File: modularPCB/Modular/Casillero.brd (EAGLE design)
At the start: 100 x 80 mm, 33 parts

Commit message: Actualización de pcbs
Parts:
- removed ALARMA, DISPONIBLE, EMISOR, LED1, LED2, LED3, OCUPADO, RECEPTOR: (no value), led:LED3MM
- removed CHAPA-DATA, CHAPA-VOL: (no value), pinhead:1X02
- removed D1: 1N4004, diode:DO41-10
- removed R-ALARMA, R-DISPONIBLE, R-GAL, R-INFRA-LED, R-OCUPADO, R-UL: 220, rcl:0204/7
- removed R-CHAPA, R-G1, R-G2: 1k, rcl:0204/7
- removed R-CHAPA2: 330, rcl:0204/7
- removed R-EMISOR: 380, rcl:0204/7
- removed R-INFRA, R-RECEPTOR: 22K, rcl:0204/7
- removed U$2: ULTRASONICO, MODULAR:ULTRASONICO
- removed U$4, U$6: 2N2222, MODULAR:2N2222
- removed U$5: RELEY, MODULAR:RELEY
- added JP2, JP3: (no value), pinhead:1X01
- added R-B, R-G, R-R: 220, rcl:0204/7
- added SG1: F/CM12P, buzzer:F/CM12P
- added SV1, SV2: (no value), con-lstb:MA04-2
- added X1, X7: 22-23-2041, con-molex:22-23-2041
- added X2, X3: 22-23-2031, con-molex:22-23-2031
- added X4, X5, X6: 22-23-2021, con-molex:22-23-2021
- JP1: device pinhead:1X03 -> pinhead:1X01
- U$3: value HX-711 -> LEDRGB; device MODULAR:HX-711 -> MODULAR:LEDRGB
- moved U$3 128.0 mm to (75.9, 22.9), turned to 90 degrees
- moved SENSADO 126.4 mm to (68.3, 11.4), turned to 270 degrees
- moved R-SENSADO 113.4 mm to (68.3, 6.35), turned to 180 degrees
- moved JP1 68.9 mm to (45.7, 12.7)
- moved U$1 66.5 mm to (38.1, 40.6), turned to 90 degrees
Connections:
- removed net DATO-CHAPA: CHAPA-DATA.1, R-CHAPA2.2, U$1.D27
- removed net DT-GALGA: U$1.D18, U$3.DT
- removed net ECHO-ULTRASONICO: U$1.D22, U$2.ECHO
- removed net GND1: U$1.GND@1
- removed net LIBRE: U$1.D15
- removed net LIBRE1: U$1.D5
- removed net LIBRE2: U$1.D25
- removed net N$1: LED1.K, R-UL.2
- removed net N$10: D1.A, U$4.C, U$5.B1
- removed net N$13: JP1.1, U$3.A+
- removed net N$14: JP1.2, R-G1.2, U$3.E-
- removed net N$15: JP1.3, R-G2.2, U$3.E+
- removed net N$16: R-G1.1, R-G2.1, U$3.A-
- removed net N$20: EMISOR.A, R-EMISOR.1
- removed net N$24: CHAPA-VOL.1, U$5.NA
- removed net N$30: R-RECEPTOR.1, RECEPTOR.K, U$6.B
- removed net N$31: LED3.A, R-INFRA-LED.1
- removed net N$32: DISPONIBLE.K, R-DISPONIBLE.2
- removed net N$33: ALARMA.K, R-ALARMA.2
- removed net N$34: R-SENSADO.2, SENSADO.K
- removed net N$8: LED2.K, R-GAL.2
- removed net N$9: R-CHAPA.1, U$4.B
- removed net PULSO-ALARMA: ALARMA.A, U$1.D14
- removed net PULSO-CHAPA: R-CHAPA.2, U$1.D26
- removed net PULSO-DISPONIBLE: DISPONIBLE.A, U$1.D12
- removed net PULSO-GALGA: LED2.A, U$1.D21
- removed net PULSO-INFRA: R-INFRA-LED.2, R-INFRA.1, U$1.D2, U$6.E
- removed net PULSO-OCUPADO: OCUPADO.A, U$1.D13
- removed net PULSO-SENSADO: SENSADO.A, U$1.D4
- removed net PULSO-ULTRASONICO: LED1.A, U$1.D32
- removed net PURA-ENTRADA: U$1.D34
- removed net SCK-GALGA: U$1.D19, U$3.SCK
- removed net TRIG-ULTRASONICO: U$1.D23, U$2.TRIG
- removed net VF: D1.C, U$5.B2, U$5.IN
- new net BUZZER: SG1.+, U$1.D27
- new net CERRADURA_CTRL: U$1.D25, X6.2
- new net CERRADURA_VCC: U$1.D26, X6.1
- new net GA_DT: U$1.D19, X3.2
- new net GA_LED: U$1.D21, X3.1
- new net GA_SCK: U$1.D18, X3.3
- new net IR: JP1.1, U$1.D34
- new net LCD_SCL: U$1.D5, X5.2
- new net LCD_SDA: U$1.D15, X5.1
- new net LED_B: R-B.2, U$1.D14, X1.4, X7.2
- new net LED_G: R-G.2, U$1.D12, X1.3, X7.3
- new net LED_R: R-R.2, U$1.D13, X1.2, X7.4
- new net N$2: R-R.1, U$3.R
- new net N$4: R-B.1, U$3.B
- new net N$7: R-SENSADO.1, SENSADO.A
- new net SENSADO_LED: JP2.1, R-SENSADO.2, U$1.D4, X4.2
- new net UL_ECHO: U$1.D22, X2.2
- new net UL_LED: U$1.D32, X2.1
- new net UL_TRG: U$1.D23, X2.3
- new net WIFI_LED: U$1.D2
- net 3V3: now also SV1.1, SV1.3, SV1.5, SV1.7; no longer CHAPA-DATA.2, R-EMISOR.2, R-RECEPTOR.2, U$3.VCC
- net GND: now also SENSADO.K, SG1.-, SV1.2, SV1.4, SV1.6, SV1.8, SV2.2, SV2.4, SV2.6, SV2.8, U$1.GND@1, X1.1, X4.1, X7.1; no longer CHAPA-VOL.2, EMISOR.K, LED3.K, R-ALARMA.1, R-CHAPA2.1, R-DISPONIBLE.1, R-GAL.1, R-INFRA.2, R-OCUPADO.1, R-SENSADO.1, R-UL.1, RECEPTOR.A, U$2.GND, U$4.E
- net N$3: now also R-G.1, U$3.G; no longer OCUPADO.K, R-OCUPADO.2
- net VIN: now also SV2.1, SV2.3, SV2.5, SV2.7; no longer U$2.VCC, U$6.C
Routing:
- net GND: track 0.00 -> 101.6 mm
- net UL_LED: track 0.00 -> 51.4 mm
- net BUZZER: track 0.00 -> 38.4 mm
- net LCD_SCL: track 0.00 -> 22.1 mm
- net VIN: track 0.00 -> 15.5 mm
- net 3V3: track 0.00 -> 15.5 mm
- net LED_R: track 0.00 -> 12.7 mm
- net LED_G: track 0.00 -> 12.7 mm
- net LED_B: track 0.00 -> 12.7 mm
- net SENSADO_LED: track 0.00 -> 8.67 mm
- net UL_TRG: track 0.00 -> 7.62 mm
- net UL_ECHO: track 0.00 -> 7.62 mm
- net LCD_SDA: track 0.00 -> 7.62 mm
- net GA_SCK: track 0.00 -> 7.62 mm
- net GA_LED: track 0.00 -> 7.62 mm
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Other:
- board size 100 x 80 mm -> 86 x 64 mm

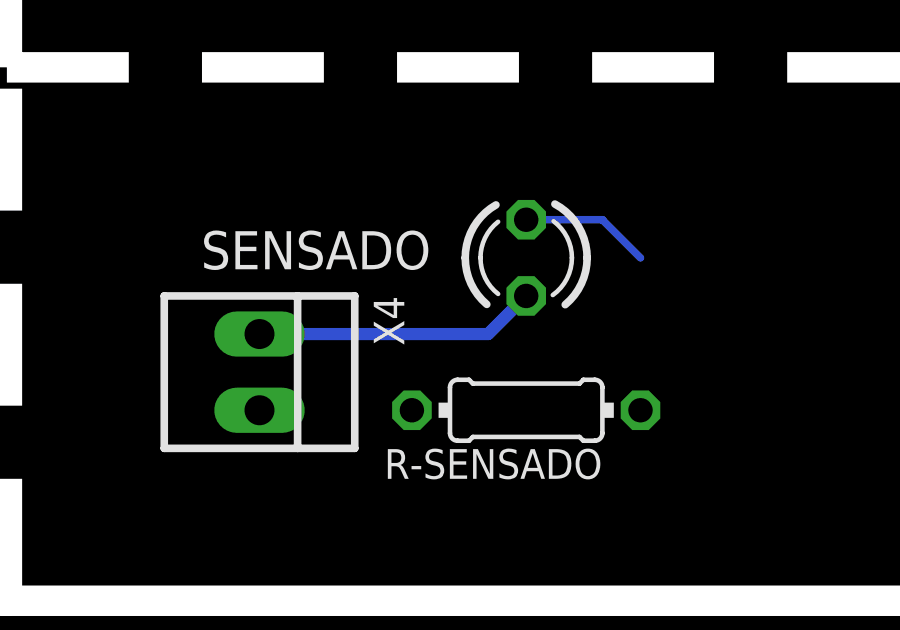
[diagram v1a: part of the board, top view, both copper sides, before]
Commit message: Corrección de errores en pcbs
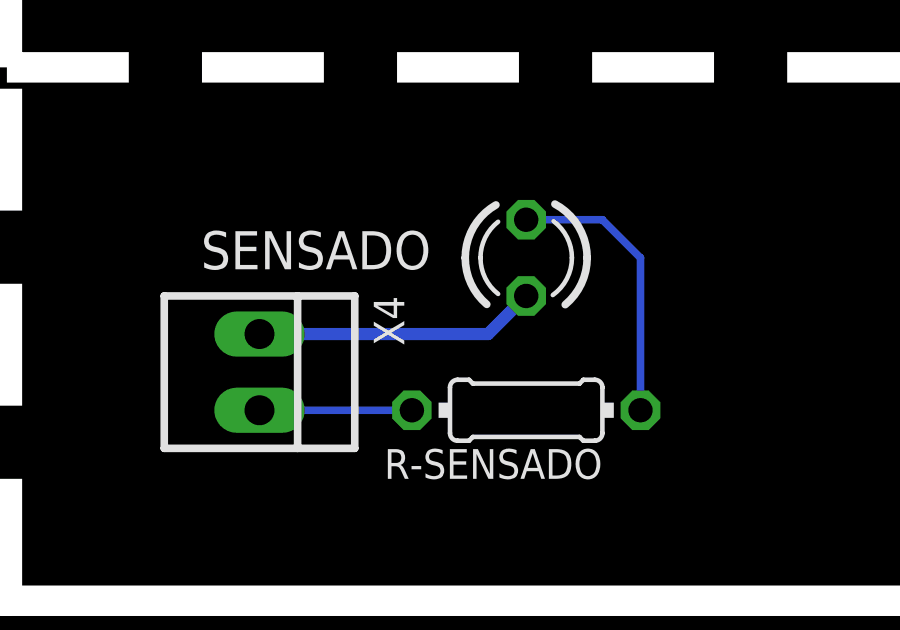
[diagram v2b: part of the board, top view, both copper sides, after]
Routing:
- net N$7: track 4.34 -> 9.42 mm
- net SENSADO_LED: track 8.67 -> 13.8 mm
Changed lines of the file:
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@@
 <wire x1="7.62" y1="30.48" x2="12.7" y2="30.48" width="0.254" layer="16"/>
 <contactref element="X4" pad="2"/>
-<wire x1="59.42" y1="6.35" x2="64.5" y2="6.35" width="0" layer="19" extent="1-1"/>
+<wire x1="64.5" y1="6.35" x2="59.42" y2="6.35" width="0.254" layer="16"/>
 <wire x1="12.7" y1="30.48" x2="59.42" y2="6.35" width="0" layer="19" extent="1-1"/>
 </signal>
@@
 <contactref element="R-SENSADO" pad="1"/>
 <wire x1="68.31" y1="12.7" x2="70.85" y2="12.7" width="0.254" layer="16"/>
-<wire x1="70.85" y1="12.7" x2="72.12" y2="11.43" width="0.254" layer="16"/>
-<wire x1="72.12" y1="6.35" x2="72.12" y2="11.43" width="0" layer="19" extent="16-16"/>
+<wire x1="72.12" y1="11.43" x2="70.85" y2="12.7" width="0.254" layer="16"/>
+<wire x1="72.12" y1="6.35" x2="72.12" y2="11.43" width="0.254" layer="16"/>
 </signal>
 </signals>

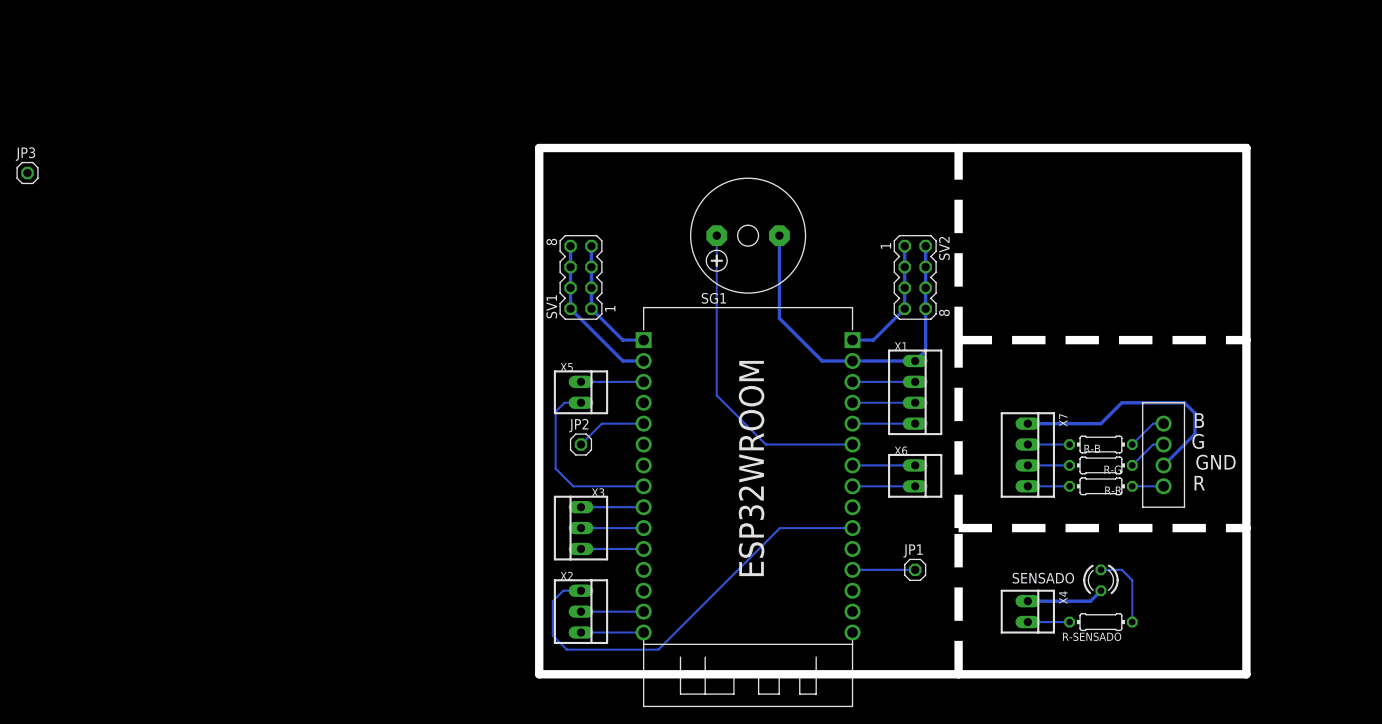
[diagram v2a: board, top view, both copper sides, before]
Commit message: Actualización de brd y grb de casillero
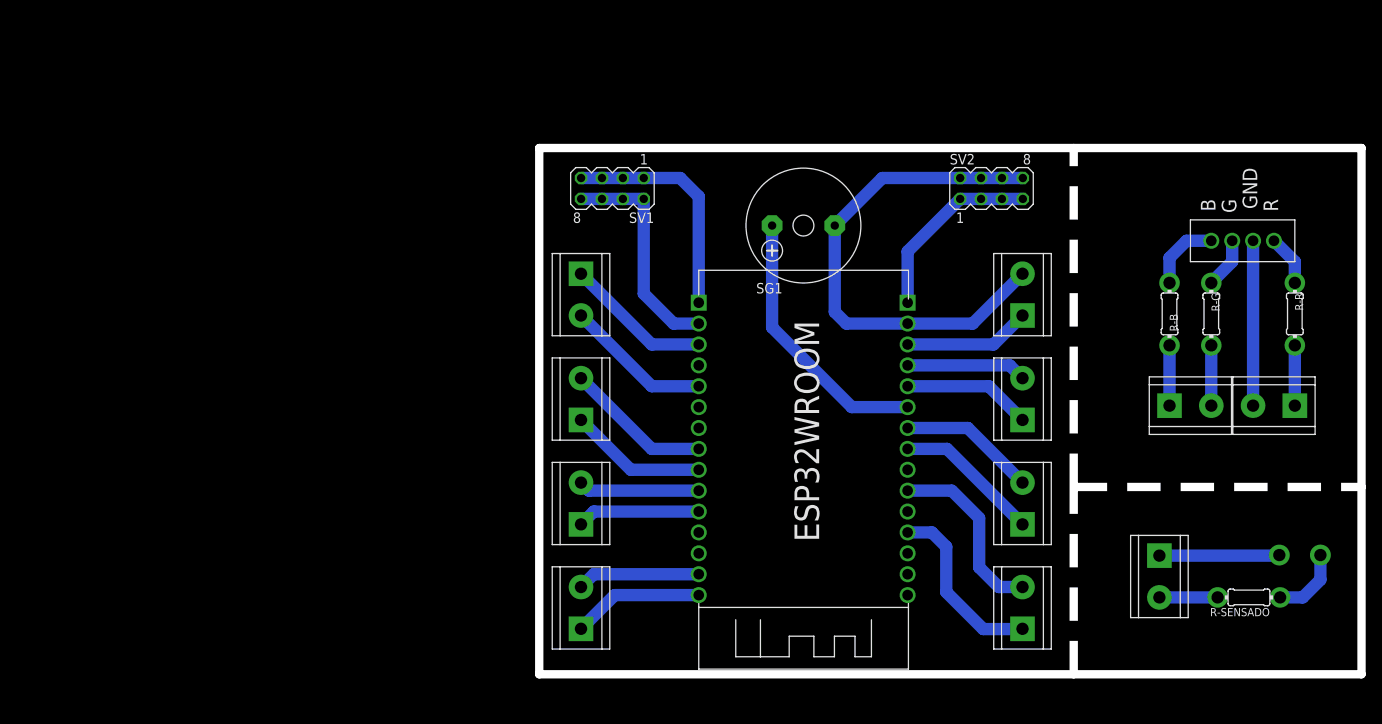
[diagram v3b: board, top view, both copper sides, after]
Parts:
- removed JP1, JP2, JP3: (no value), pinhead:1X01
- removed SENSADO: (no value), led:LED3MM
- removed X1, X7: 22-23-2041, con-molex:22-23-2041
- removed X2, X3: 22-23-2031, con-molex:22-23-2031
- removed X4, X5, X6: 22-23-2021, con-molex:22-23-2021
- added U$10, U$11, U$12, U$13, U$2, U$4, U$5, U$6, U$7, U$8, U$9: CLEMAS, MODULAR:CLEMAS
- moved U$3 32.7 mm to (89.3, 52.7), turned to 180 degrees
- moved R-R 31.6 mm to (91.9, 43.8), turned to 270 degrees
- moved R-G 22.8 mm to (81.7, 43.8), turned to 270 degrees
- moved R-SENSADO 18.2 mm to (86.3, 9.35)
- moved R-B 17.9 mm to (76.7, 43.8), turned to 270 degrees
- moved U$1 14.8 mm to (33.4, 26.6)
- moved SV2 14.3 mm to (55.0, 59.1), turned to 0 degrees
- moved SV1 11.5 mm to (8.90, 59.1), turned to 180 degrees
- moved SG1 6.84 mm to (32.1, 54.6)
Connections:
- net CERRADURA_CTRL: now also U$8.1; no longer X6.2
- net CERRADURA_VCC: now also U$8.2; no longer X6.1
- net GA_DT: now also U$4.2; no longer X3.2
- net GA_LED: now also U$4.1; no longer X3.1
- net GA_SCK: now also U$5.1; no longer X3.3
- net GND: now also U$10.2, U$12.2, U$13.1; no longer SENSADO.K, X1.1, X4.1, X7.1
- net IR: now also U$7.1; no longer JP1.1
- net LCD_SCL: now also U$5.2; no longer X5.2
- net LCD_SDA: now also U$6.1; no longer X5.1
- net LED_B: now also U$11.1, U$9.1; no longer X1.4, X7.2
- net LED_G: now also U$11.2, U$9.2; no longer X1.3, X7.3
- net LED_R: now also U$10.1, U$12.1; no longer X1.2, X7.4
- net N$7: no longer SENSADO.A
- net SENSADO_LED: now also U$13.2, U$6.2; no longer JP2.1, X4.2
- net UL_ECHO: now also U$2.2; no longer X2.2
- net UL_LED: now also U$7.2; no longer X2.1
- net UL_TRG: now also U$2.1; no longer X2.3
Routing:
- net UL_LED: track 51.4 -> 22.3 mm
- net GND: track 101.6 -> 123.7 mm, vias 0 -> 1
- net IR: track 7.62 -> 22.1 mm
- net 3V3: track 15.5 -> 28.2 mm
- net SENSADO_LED: track 13.8 -> 25.0 mm, vias 0 -> 1
- net LED_B: track 12.7 -> 23.0 mm, vias 0 -> 1
- net LCD_SDA: track 7.62 -> 17.9 mm
- net CERRADURA_CTRL: track 7.62 -> 17.8 mm
- net LED_R: track 12.7 -> 22.8 mm, vias 0 -> 1
- net LED_G: track 12.7 -> 22.0 mm, vias 0 -> 1
- net GA_SCK: track 7.62 -> 16.8 mm
- net CERRADURA_VCC: track 7.62 -> 16.7 mm
- net UL_TRG: track 7.62 -> 16.0 mm
- net UL_ECHO: track 7.62 -> 15.0 mm
- net GA_LED: track 7.62 -> 15.0 mm
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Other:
- board size 86 x 64 mm -> 100 x 64 mm
